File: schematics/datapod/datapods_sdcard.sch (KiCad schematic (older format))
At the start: 3 parts, among them J3 Micro_SD_Card, U3 74LVC125

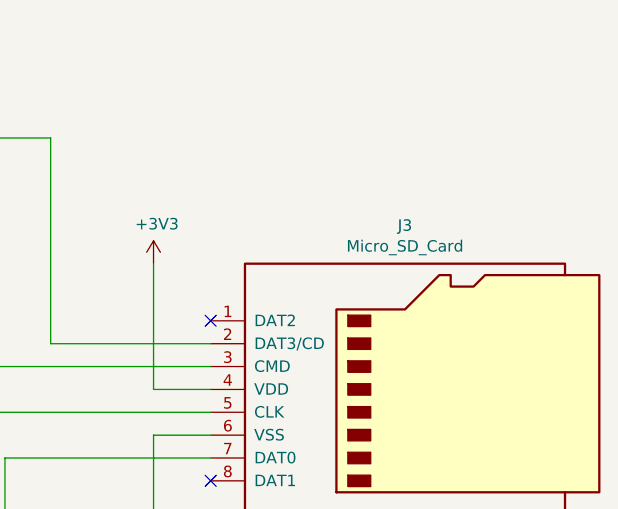
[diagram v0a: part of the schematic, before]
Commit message: added more connectors and started drawing the PCB
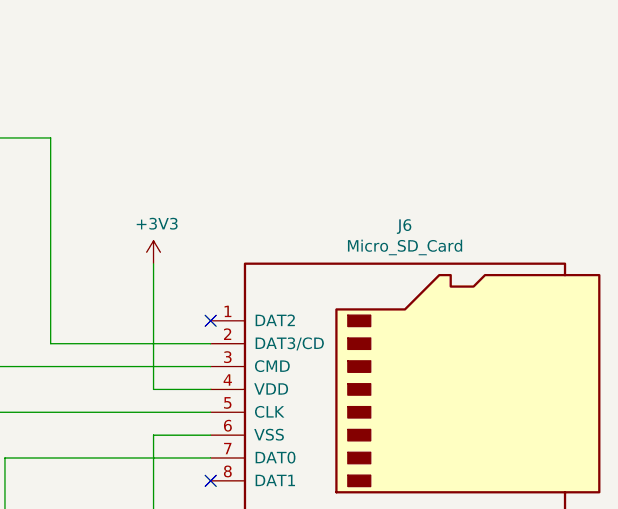
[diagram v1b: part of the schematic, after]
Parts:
- renumbered J3 to J6
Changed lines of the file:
@@
 $EndComp
 $Comp
-L Connector:Micro_SD_Card J3
+L Connector:Micro_SD_Card J6
 U 1 1 5E48AC0F
 P 8650 3400
-F 0 "J3" H 8600 4117 50  0000 C CNN
+F 0 "J6" H 8600 4117 50  0000 C CNN
 F 1 "Micro_SD_Card" H 8600 4026 50  0000 C CNN
 F 2 "Connector_Card:microSD_HC_Wuerth_693072010801" H 9800 3700 50  0001 C CNN
@@
 	2650 4750 2150 4750
 $Comp
-L power:+3V3 #PWR0125
+L power:+3V3 #PWR028
 U 1 1 5E4DE9E0
 P 1500 2000
-F 0 "#PWR0125" H 1500 1850 50  0001 C CNN
+F 0 "#PWR028" H 1500 1850 50  0001 C CNN
 F 1 "+3V3" H 1515 2173 50  0000 C CNN
 F 2 "" H 1500 2000 50  0001 C CNN
@@
 $EndComp
 $Comp
-L power:GND #PWR0126
+L power:GND #PWR031
 U 1 1 5E4DF563
 P 1500 3450
-F 0 "#PWR0126" H 1500 3200 50  0001 C CNN
+F 0 "#PWR031" H 1500 3200 50  0001 C CNN
 F 1 "GND" H 1505 3277 50  0000 C CNN
 F 2 "" H 1500 3450 50  0001 C CNN
@@
 NoConn ~ 7750 3800
 $Comp
-L power:+3V3 #PWR0127
+L power:+3V3 #PWR030
 U 1 1 5E4E3BF5
 P 7500 2850
-F 0 "#PWR0127" H 7500 2700 50  0001 C CNN
+F 0 "#PWR030" H 7500 2700 50  0001 C CNN
 F 1 "+3V3" H 7515 3023 50  0000 C CNN
 F 2 "" H 7500 2850 50  0001 C CNN
@@
 $EndComp
 $Comp
-L power:GND #PWR0128
+L power:GND #PWR033
 U 1 1 5E4E4242
 P 7500 4450
-F 0 "#PWR0128" H 7500 4200 50  0001 C CNN
+F 0 "#PWR033" H 7500 4200 50  0001 C CNN
 F 1 "GND" H 7505 4277 50  0000 C CNN
 F 2 "" H 7500 4450 50  0001 C CNN
@@
 	7500 3400 7500 2850
 $Comp
-L power:GND #PWR0129
+L power:GND #PWR032
 U 1 1 5E4E7A83
 P 6250 3450
-F 0 "#PWR0129" H 6250 3200 50  0001 C CNN
+F 0 "#PWR032" H 6250 3200 50  0001 C CNN
 F 1 "GND" H 6255 3277 50  0000 C CNN
 F 2 "" H 6250 3450 50  0001 C CNN
@@
 $EndComp
 $Comp
-L power:GND #PWR0130
+L power:GND #PWR034
 U 1 1 5E4E7CFA
 P 6250 4550
-F 0 "#PWR0130" H 6250 4300 50  0001 C CNN
+F 0 "#PWR034" H 6250 4300 50  0001 C CNN
 F 1 "GND" H 6255 4377 50  0000 C CNN
 F 2 "" H 6250 4550 50  0001 C CNN
@@
 $EndComp
 $Comp
-L power:GND #PWR0131
+L power:GND #PWR029
 U 1 1 5E4E825B
 P 6250 2600
-F 0 "#PWR0131" H 6250 2350 50  0001 C CNN
+F 0 "#PWR029" H 6250 2350 50  0001 C CNN
 F 1 "GND" H 6255 2427 50  0000 C CNN
 F 2 "" H 6250 2600 50  0001 C CNN
@@
 	6250 4450 6250 4550
 $Comp
-L power:GND #PWR0132
+L power:GND #PWR035
 U 1 1 5E4EAF1B
 P 2950 5350
-F 0 "#PWR0132" H 2950 5100 50  0001 C CNN
+F 0 "#PWR035" H 2950 5100 50  0001 C CNN
 F 1 "GND" H 2955 5177 50  0000 C CNN
 F 2 "" H 2950 5350 50  0001 C CNN

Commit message: replaced rn2 with 4 resistors and moved sd card closer to mcu
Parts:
- removed RN2: 3.3K, Resistor_SMD:R_Array_Convex_4x1206, symbol Device:R_Pack04
- added R5, R6, R7, R8: 3.3K, Resistor_SMD:R_1206_3216Metric_Pad1.42x1.75mm_HandSolder, symbol Device:R
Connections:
- wire segments 45 -> 47
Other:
- note added: "DAT2/X\nDAT3/CS\nCMD/DI\nVDD/VDD\nCLK/SCLK\nVSS/VSS\nDAT0/ D0\nDAT1/ X"
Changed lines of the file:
@@
 EESchema Schematic File Version 4
-LIBS:datapod-cache
+LIBS:_autosave-datapod-cache
 EELAYER 30 0
 EELAYER END
@@
 	1    0    0    -1
 $EndComp
-$Comp
-L Device:R_Pack04 RN2
-U 1 1 5E49AE7B
-P 4750 4000
-F 0 "RN2" V 4333 4000 50  0000 C CNN
-F 1 "3.3K" V 4424 4000 50  0000 C CNN
-F 2 "Resistor_SMD:R_Array_Convex_4x1206" V 5025 4000 50  0001 C CNN
-F 3 "https://www.bourns.com/docs/Product-Datasheets/CATCAY.pdf" H 4750 4000 50  0001 C CNN
-F 4 "Digikey" V 4750 4000 50  0001 C CNN "Vendor"
-F 5 "CAY16-332J4LFCT-ND" V 4750 4000 50  0001 C CNN "Part#"
-	1    4750 4000
-	0    1    1    0
-$EndComp
 Text GLabel 3450 3900 0    50   Input ~ 0
 MICRO_SD_MOSI
@@
 Wire Wire Line
 	6850 3700 6850 5300
-Wire Wire Line
-	4950 4100 4950 5300
-Wire Wire Line
-	4950 5300 6850 5300
 Wire Wire Line
 	4550 4100 4050 4100
@@
 	4550 4000 3450 4000
 Wire Wire Line
-	4950 4000 5350 4000
-Wire Wire Line
 	5350 4000 5350 4200
 Wire Wire Line
@@
 Wire Wire Line
 	5200 3100 5200 3900
-Wire Wire Line
-	5200 3900 4950 3900
 Wire Wire Line
 	3450 3800 4550 3800
@@
 Wire Wire Line
 	9450 4000 9450 4300
+Wire Wire Line
+	5250 5300 6850 5300
+Wire Wire Line
+	5250 4100 5250 5300
+$Comp
+L Device:R R5
+U 1 1 5DDEF8A9
+P 4700 3800
+F 0 "R5" V 4650 3400 50  0000 C CNN
+F 1 "3.3K" V 4650 3550 50  0000 C CNN
+F 2 "Resistor_SMD:R_1206_3216Metric_Pad1.42x1.75mm_HandSolder" V 4630 3800 50  0001 C CNN
+F 3 "https://www.te.com/commerce/DocumentDelivery/DDEController?Action=srchrtrv&DocNm=9-1773463-9&DocType=DS&DocLang=English" H 4700 3800 50  0001 C CNN
+F 4 "Digikey" V 4700 3800 50  0001 C CNN "Vendor"
+F 5 "A130544CT-ND" V 4700 3800 50  0001 C CNN "Part#"
+	1    4700 3800
+	0    1    1    0
+$EndComp
+Wire Wire Line
+	4950 3800 4850 3800
+$Comp
+L Device:R R7
+U 1 1 5DDF39E5
+P 4700 4000
+F 0 "R7" V 4650 3600 50  0000 C CNN
+F 1 "3.3K" V 4650 3750 50  0000 C CNN
+F 2 "Resistor_SMD:R_1206_3216Metric_Pad1.42x1.75mm_HandSolder" V 4630 4000 50  0001 C CNN
+F 3 "https://www.te.com/commerce/DocumentDelivery/DDEController?Action=srchrtrv&DocNm=9-1773463-9&DocType=DS&DocLang=English" H 4700 4000 50  0001 C CNN
+F 4 "Digikey" V 4700 4000 50  0001 C CNN "Vendor"
+F 5 "A130544CT-ND" V 4700 4000 50  0001 C CNN "Part#"
+	1    4700 4000
+	0    1    1    0
+$EndComp
+$Comp
+L Device:R R8
+U 1 1 5DDF3C58
+P 4700 4100
+F 0 "R8" V 4650 3700 50  0000 C CNN
+F 1 "3.3K" V 4650 3850 50  0000 C CNN
+F 2 "Resistor_SMD:R_1206_3216Metric_Pad1.42x1.75mm_HandSolder" V 4630 4100 50  0001 C CNN
+F 3 "https://www.te.com/commerce/DocumentDelivery/DDEController?Action=srchrtrv&DocNm=9-1773463-9&DocType=DS&DocLang=English" H 4700 4100 50  0001 C CNN
+F 4 "Digikey" V 4700 4100 50  0001 C CNN "Vendor"
+F 5 "A130544CT-ND" V 4700 4100 50  0001 C CNN "Part#"
+	1    4700 4100
+	0    1    1    0
+$EndComp
+$Comp
+L Device:R R6
+U 1 1 5DDF37A5
+P 4700 3900
+F 0 "R6" V 4650 3500 50  0000 C CNN
+F 1 "3.3K" V 4650 3650 50  0000 C CNN
+F 2 "Resistor_SMD:R_1206_3216Metric_Pad1.42x1.75mm_HandSolder" V 4630 3900 50  0001 C CNN
+F 3 "https://www.te.com/commerce/DocumentDelivery/DDEController?Action=srchrtrv&DocNm=9-1773463-9&DocType=DS&DocLang=English" H 4700 3900 50  0001 C CNN
+F 4 "Digikey" V 4700 3900 50  0001 C CNN "Vendor"
+F 5 "A130544CT-ND" V 4700 3900 50  0001 C CNN "Part#"
+	1    4700 3900
+	0    1    1    0
+$EndComp
+Wire Wire Line
+	4850 3900 5200 3900
+Wire Wire Line
+	4850 4000 5350 4000
+Wire Wire Line
+	4850 4100 5250 4100
+Text Notes 9650 3600 0    59   ~ 0
+DAT2/X\nDAT3/CS\nCMD/DI\nVDD/VDD\nCLK/SCLK\nVSS/VSS\nDAT0/ D0\nDAT1/ X
 $EndSCHEMATC

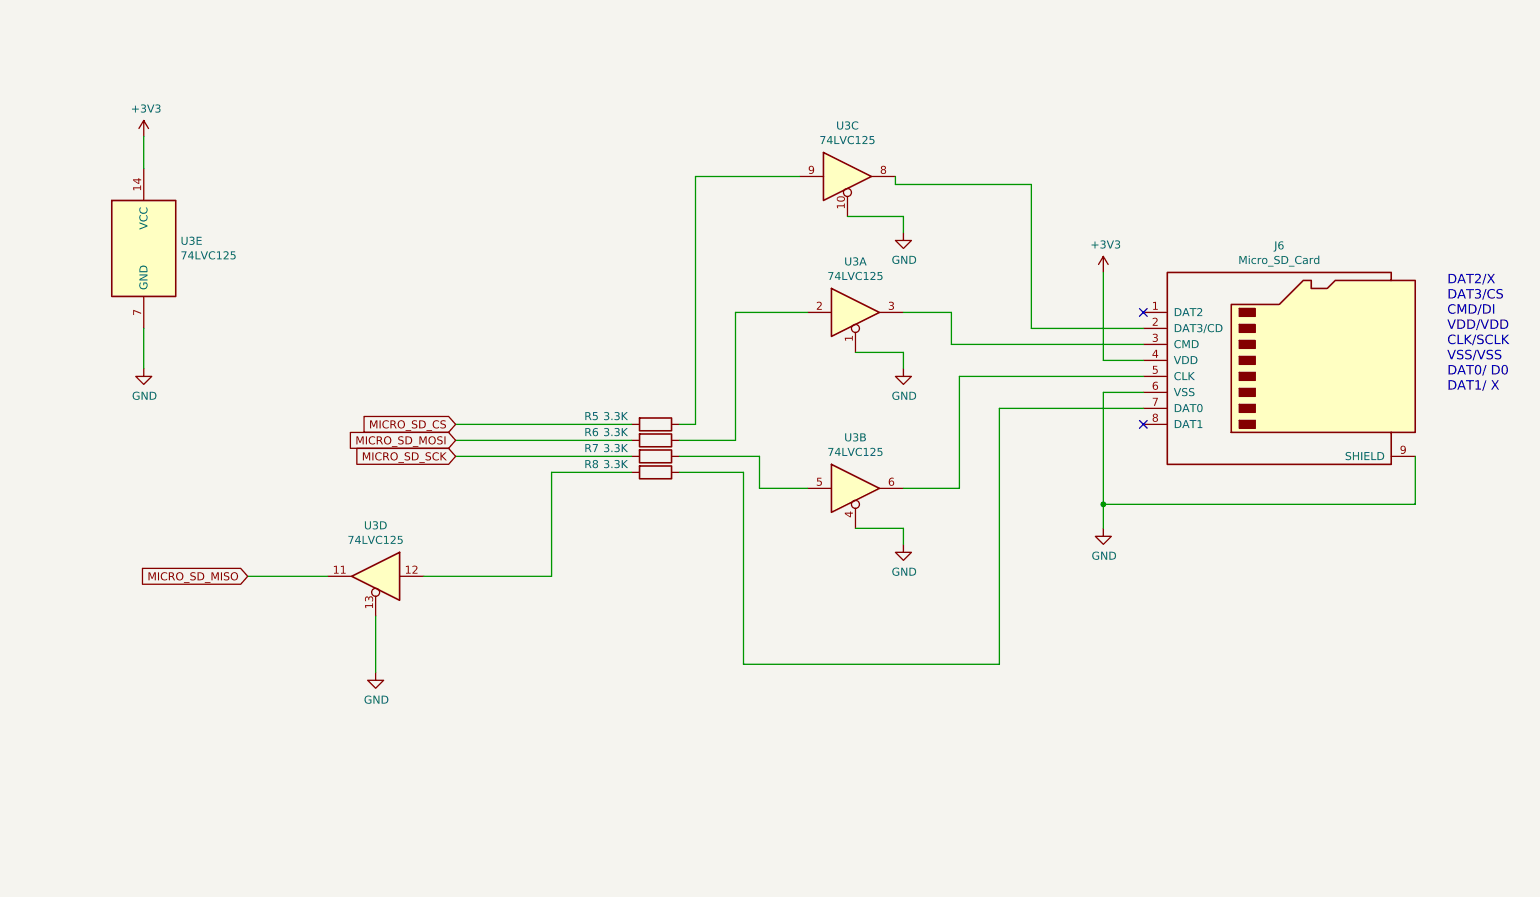
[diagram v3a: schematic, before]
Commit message: fixed bad gnd trace on 3.3v circuit and added comments to the silkscreen
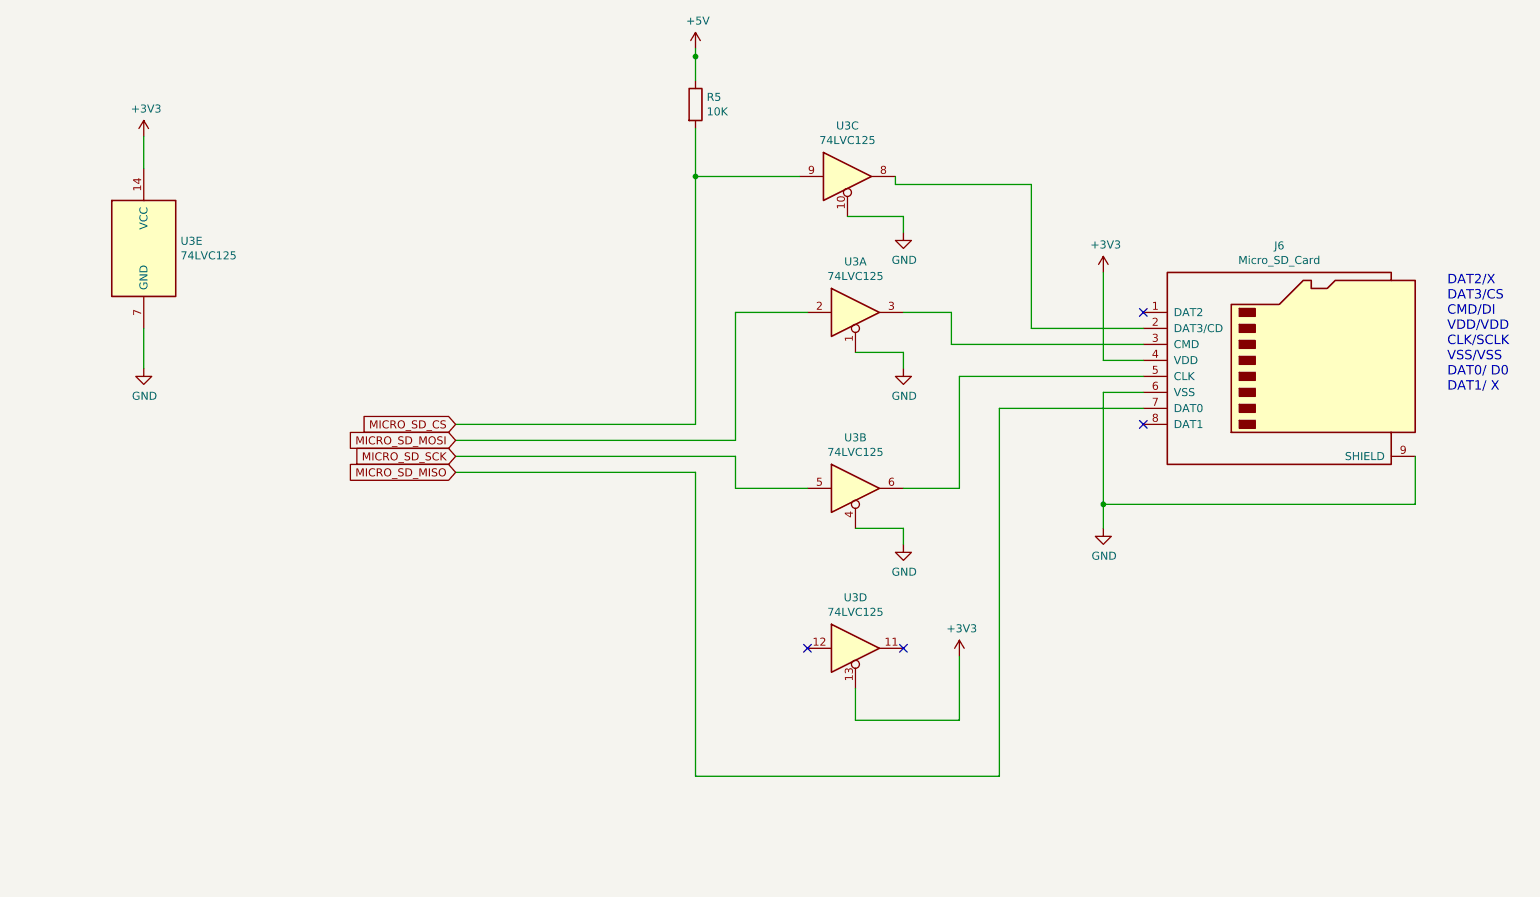
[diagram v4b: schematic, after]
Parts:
- removed R6, R7, R8: 3.3K, Resistor_SMD:R_1206_3216Metric_Pad1.42x1.75mm_HandSolder, symbol Device:R
- R5: value 3.3K -> 10K; Part# A130544CT-ND -> (none); part# (none) -> 749-1125-6-ND
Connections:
- net +3V3: now also U3.13
- net GND: no longer U3.13
- net MICRO_SD_CS: now also U3.9
- net MICRO_SD_MISO: now also J6.7 (DAT0); no longer U3.11
- net MICRO_SD_MOSI: now also U3.2
- net MICRO_SD_SCK: now also U3.5
- net +5V: now reaches R5.1
- net +5V: no longer U3.9
- no-connect marks 2 -> 4
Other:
- moved on the sheet: U3D
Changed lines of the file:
@@
 MICRO_SD_SCK
-Wire Wire Line
-	3450 3900 4550 3900
 Wire Wire Line
 	6250 4200 6600 4200
@@
 Wire Wire Line
 	7750 3700 6850 3700
-Wire Wire Line
-	6850 3700 6850 5300
-Wire Wire Line
-	4550 4100 4050 4100
-Wire Wire Line
-	4050 4100 4050 4750
-Wire Wire Line
-	4050 4750 3250 4750
-Text GLabel 2150 4750 0    50   Input ~ 0
+Text GLabel 3450 4100 0    50   Input ~ 0
 MICRO_SD_MISO
-Wire Wire Line
-	2650 4750 2150 4750
 $Comp
 L power:+3V3 #PWR028
@@
 $EndComp
 Wire Wire Line
-	5900 2500 6250 2500
-Wire Wire Line
-	6250 2500 6250 2600
-Wire Wire Line
 	5950 3350 6250 3350
 Wire Wire Line
@@
 Wire Wire Line
 	6250 4450 6250 4550
-$Comp
-L power:GND #PWR035
-U 1 1 5E4EAF1B
-P 2950 5350
-F 0 "#PWR035" H 2950 5100 50  0001 C CNN
-F 1 "GND" H 2955 5177 50  0000 C CNN
-F 2 "" H 2950 5350 50  0001 C CNN
-F 3 "" H 2950 5350 50  0001 C CNN
-	1    2950 5350
-	1    0    0    -1
-$EndComp
-Wire Wire Line
-	2950 5000 2950 5350
-Wire Wire Line
-	4550 4000 3450 4000
-Wire Wire Line
-	5350 4000 5350 4200
-Wire Wire Line
-	5350 4200 5650 4200
 Wire Wire Line
 	5650 3100 5200 3100
 Wire Wire Line
 	5200 3100 5200 3900
-Wire Wire Line
-	3450 3800 4550 3800
 Wire Wire Line
 	4950 3800 4950 2250
@@
 L 74xx:74LVC125 U3
 U 4 1 5E5439BD
-P 2950 4750
-F 0 "U3" H 2950 5067 50  0000 C CNN
-F 1 "74LVC125" H 2950 4976 50  0000 C CNN
-F 2 "Package_SO:TSSOP-14_4.4x5mm_P0.65mm" H 2950 4750 50  0001 C CNN
-F 3 "http://www.ti.com/general/docs/suppproductinfo.tsp?distId=10&gotoUrl=http%3A%2F%2Fwww.ti.com%2Flit%2Fgpn%2Fsn74lvc125a" H 2950 4750 50  0001 C CNN
-F 4 "Digikey" H 2950 4750 50  0001 C CNN "Vendor"
-F 5 "296-1222-1-ND" H 2950 4750 50  0001 C CNN "Part#"
-	4    2950 4750
-	-1   0    0    -1
+P 5950 5200
+F 0 "U3" H 5950 5517 50  0000 C CNN
+F 1 "74LVC125" H 5950 5426 50  0000 C CNN
+F 2 "Package_SO:TSSOP-14_4.4x5mm_P0.65mm" H 5950 5200 50  0001 C CNN
+F 3 "http://www.ti.com/general/docs/suppproductinfo.tsp?distId=10&gotoUrl=http%3A%2F%2Fwww.ti.com%2Flit%2Fgpn%2Fsn74lvc125a" H 5950 5200 50  0001 C CNN
+F 4 "Digikey" H 5950 5200 50  0001 C CNN "Vendor"
+F 5 "296-1222-1-ND" H 5950 5200 50  0001 C CNN "Part#"
+	4    5950 5200
+	1    0    0    -1
 $EndComp
 Wire Wire Line
 	9450 4000 9450 4300
-Wire Wire Line
-	5250 5300 6850 5300
-Wire Wire Line
-	5250 4100 5250 5300
-$Comp
-L Device:R R5
-U 1 1 5DDEF8A9
-P 4700 3800
-F 0 "R5" V 4650 3400 50  0000 C CNN
-F 1 "3.3K" V 4650 3550 50  0000 C CNN
-F 2 "Resistor_SMD:R_1206_3216Metric_Pad1.42x1.75mm_HandSolder" V 4630 3800 50  0001 C CNN
-F 3 "https://www.te.com/commerce/DocumentDelivery/DDEController?Action=srchrtrv&DocNm=9-1773463-9&DocType=DS&DocLang=English" H 4700 3800 50  0001 C CNN
-F 4 "Digikey" V 4700 3800 50  0001 C CNN "Vendor"
-F 5 "A130544CT-ND" V 4700 3800 50  0001 C CNN "Part#"
-	1    4700 3800
-	0    1    1    0
-$EndComp
-Wire Wire Line
-	4950 3800 4850 3800
-$Comp
-L Device:R R7
-U 1 1 5DDF39E5
-P 4700 4000
-F 0 "R7" V 4650 3600 50  0000 C CNN
-F 1 "3.3K" V 4650 3750 50  0000 C CNN
-F 2 "Resistor_SMD:R_1206_3216Metric_Pad1.42x1.75mm_HandSolder" V 4630 4000 50  0001 C CNN
-F 3 "https://www.te.com/commerce/DocumentDelivery/DDEController?Action=srchrtrv&DocNm=9-1773463-9&DocType=DS&DocLang=English" H 4700 4000 50  0001 C CNN
-F 4 "Digikey" V 4700 4000 50  0001 C CNN "Vendor"
-F 5 "A130544CT-ND" V 4700 4000 50  0001 C CNN "Part#"
-	1    4700 4000
-	0    1    1    0
-$EndComp
-$Comp
-L Device:R R8
-U 1 1 5DDF3C58
-P 4700 4100
-F 0 "R8" V 4650 3700 50  0000 C CNN
-F 1 "3.3K" V 4650 3850 50  0000 C CNN
-F 2 "Resistor_SMD:R_1206_3216Metric_Pad1.42x1.75mm_HandSolder" V 4630 4100 50  0001 C CNN
-F 3 "https://www.te.com/commerce/DocumentDelivery/DDEController?Action=srchrtrv&DocNm=9-1773463-9&DocType=DS&DocLang=English" H 4700 4100 50  0001 C CNN
-F 4 "Digikey" V 4700 4100 50  0001 C CNN "Vendor"
-F 5 "A130544CT-ND" V 4700 4100 50  0001 C CNN "Part#"
-	1    4700 4100
-	0    1    1    0
-$EndComp
-$Comp
-L Device:R R6
-U 1 1 5DDF37A5
-P 4700 3900
-F 0 "R6" V 4650 3500 50  0000 C CNN
-F 1 "3.3K" V 4650 3650 50  0000 C CNN
-F 2 "Resistor_SMD:R_1206_3216Metric_Pad1.42x1.75mm_HandSolder" V 4630 3900 50  0001 C CNN
-F 3 "https://www.te.com/commerce/DocumentDelivery/DDEController?Action=srchrtrv&DocNm=9-1773463-9&DocType=DS&DocLang=English" H 4700 3900 50  0001 C CNN
-F 4 "Digikey" V 4700 3900 50  0001 C CNN "Vendor"
-F 5 "A130544CT-ND" V 4700 3900 50  0001 C CNN "Part#"
-	1    4700 3900
-	0    1    1    0
-$EndComp
-Wire Wire Line
-	4850 3900 5200 3900
-Wire Wire Line
-	4850 4000 5350 4000
-Wire Wire Line
-	4850 4100 5250 4100
 Text Notes 9650 3600 0    59   ~ 0
 DAT2/X\nDAT3/CS\nCMD/DI\nVDD/VDD\nCLK/SCLK\nVSS/VSS\nDAT0/ D0\nDAT1/ X
+Wire Wire Line
+	3450 3800 4950 3800
+Wire Wire Line
+	3450 3900 5200 3900
+Wire Wire Line
+	6850 6000 4950 6000
+Wire Wire Line
+	4950 6000 4950 4100
+Wire Wire Line
+	4950 4100 3450 4100
+Wire Wire Line
+	6850 3700 6850 6000
+Wire Wire Line
+	3450 4000 5200 4000
+Wire Wire Line
+	5200 4000 5200 4200
+Wire Wire Line
+	5200 4200 5650 4200
+NoConn ~ 6250 5200
+NoConn ~ 5650 5200
+$Comp
+L power:+3V3 #PWR0109
+U 1 1 5E1D8642
+P 6600 5250
+F 0 "#PWR0109" H 6600 5100 50  0001 C CNN
+F 1 "+3V3" H 6615 5423 50  0000 C CNN
+F 2 "" H 6600 5250 50  0001 C CNN
+F 3 "" H 6600 5250 50  0001 C CNN
+	1    6600 5250
+	1    0    0    -1
+$EndComp
+Wire Wire Line
+	5950 5450 5950 5650
+Wire Wire Line
+	5950 5650 6600 5650
+Wire Wire Line
+	6600 5650 6600 5250
+Wire Wire Line
+	5900 2500 6250 2500
+Wire Wire Line
+	6250 2500 6250 2600
+$Comp
+L Device:R R5
+U 1 1 5E20A2C5
+P 4950 1800
+F 0 "R5" H 5020 1846 50  0000 L CNN
+F 1 "10K" H 5020 1755 50  0000 L CNN
+F 2 "Resistor_SMD:R_1206_3216Metric_Pad1.42x1.75mm_HandSolder" V 4880 1800 50  0001 C CNN
+F 3 "http://www.vishay.com/docs/28796/mcw0406atpro.pdf" H 4950 1800 50  0001 C CNN
+F 4 "Digikey" H 4950 1800 50  0001 C CNN "Vendor"
+F 5 "749-1125-6-ND" H 4950 1800 50  0001 C CNN "part#"
+	1    4950 1800
+	1    0    0    -1
+$EndComp
+Wire Wire Line
+	4950 1950 4950 2250
+Connection ~ 4950 2250
+Wire Wire Line
+	4950 1450 4950 1500
+$Comp
+L power:+5V #PWR?
+U 1 1 5E216351
+P 4950 1450
+AR Path="/5E216351" Ref="#PWR?"  Part="1"
+AR Path="/5E3A21FB/5E216351" Ref="#PWR01"  Part="1"
+F 0 "#PWR01" H 4950 1300 50  0001 C CNN
+F 1 "+5V" H 4965 1623 50  0000 C CNN
+F 2 "" H 4950 1450 50  0001 C CNN
+F 3 "" H 4950 1450 50  0001 C CNN
+	1    4950 1450
+	1    0    0    -1
+$EndComp
+Connection ~ 4950 1500
+Wire Wire Line
+	4950 1500 4950 1650
 $EndSCHEMATC
